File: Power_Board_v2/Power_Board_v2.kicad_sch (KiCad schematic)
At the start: 33 parts, among them J1 Conn_02x16_Odd_Even, Q1 MMBT5551L, U2 HUSB237-AA001-DN06R, U3 BQ24074RGT, U4 INA219AxDCN SOT-23

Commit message: misc.
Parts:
- C4, C8: LCSC (none) -> C19666; Supplier Part C19666 -> (none)
- C5, C6, C7: LCSC (none) -> C15849; Supplier Part C15849 -> (none)
- D1: LCSC (none) -> C2290; Supplier Part C2290 -> (none)
- D2: LCSC (none) -> C2286; Supplier Part C2286 -> (none)
- Q1: LCSC (none) -> C2145; Supplier Part C2145 -> (none)
- R10, R16: LCSC (none) -> C25804; Supplier Part C25804 -> (none)
- R11, R12, R13, R15, R18, R9: LCSC (none) -> C22843; Supplier Part C22843 -> (none)
- R14, R17: LCSC (none) -> C333100; Supplier Part C333100 -> (none)
- R2: LCSC (none) -> C23242; Supplier Part C19666 -> (none)
- R3: LCSC (none) -> C23159; Supplier Part C23159 -> (none)
- R4: LCSC (none) -> C17471
- R7: LCSC (none) -> C25804
- U2: LCSC (none) -> C22373734; SUPPLIER PART C22373734 -> (none)
- U3: LCSC (none) -> C54313; Supplier Part C54313 -> (none)
- U4: LCSC (none) -> C87469; Supplier Part C87469 -> (none)
- USBC1: LCSC (none) -> C165948; Supplier Part C165948 -> (none)
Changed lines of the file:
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@@
 			)
 		)
+		(property "LCSC" "C25804"
+			(at 195.58 60.96 0)
+			(effects
+				(font
+					(size 1.27 1.27)
+				)
+				(hide yes)
+			)
+		)
 		(pin "2"
 		)
@@
 			)
 		)
-		(property "Supplier Part" "C25804"
+		(property "LCSC" "C25804"
 			(at 71.12 40.64 0)
 			(effects
@@
 			)
 		)
-		(property "Supplier Part" "C22843"
+		(property "LCSC" "C22843"
 			(at 148.59 53.34 0)
 			(effects
@@
 			)
 		)
-		(property "Supplier Part" "C19666"
+		(property "LCSC" "C19666"
 			(at 190.5 58.42 0)
 			(effects
@@
 			)
 		)
-		(property "Supplier Part" "C165948"
+		(property "LCSC" "C165948"
 			(at 34.29 135.89 0)
 			(effects
@@
 			)
 		)
-		(property "Supplier Part" "C15849"
+		(property "LCSC" "C15849"
 			(at 148.59 27.94 0)
 			(effects
@@
 			)
 		)
-		(property "Supplier Part" "C22843"
+		(property "LCSC" "C22843"
 			(at 148.59 48.26 0)
 			(effects
@@
 			)
 		)
-		(property "Supplier Part" "C25804"
+		(property "LCSC" "C25804"
 			(at 71.12 64.77 0)
 			(effects
@@
 			)
 		)
-		(property "Supplier Part" "C87469"
+		(property "LCSC" "C87469"
 			(at 58.42 52.07 0)
 			(effects
@@
 			)
 		)
-		(property "Supplier Part" "C22843"
+		(property "LCSC" "C22843"
 			(at 157.48 88.9 0)
 			(effects
@@
 			)
 		)
-		(property "Supplier Part" "C2286"
+		(property "LCSC" "C2286"
 			(at 201.93 43.18 90)
 			(effects
@@
 			)
 		)
-		(property "Supplier Part" "C22843"
+		(property "LCSC" "C22843"
 			(at 201.93 35.56 0)
 			(effects
@@
 			)
 		)
+		(property "LCSC" "C17471"
+			(at 143.51 76.2 0)
+			(effects
+				(font
+					(size 1.27 1.27)
+				)
+				(hide yes)
+			)
+		)
 		(pin "2"
 		)
@@
 			)
 		)
-		(property "Supplier Part" " C2145"
+		(property "LCSC" " C2145"
 			(at 154.94 67.31 0)
 			(effects
@@
 			)
 		)
-		(property "SUPPLIER PART" "C22373734"
+		(property "LCSC" "C22373734"
 			(at 81.28 137.16 0)
 			(effects
@@
 			)
 		)
-		(property "Supplier Part" "C15849"
+		(property "LCSC" "C15849"
 			(at 78.74 54.61 0)
 			(effects
@@
 			)
 		)
-		(property "Supplier Part" "C23159"
+		(property "LCSC" "C23159"
 			(at 143.51 62.23 0)
 			(effects
@@
 			)
 		)
-		(property "Supplier Part" "C19666"
+		(property "LCSC" "C19666"
 			(at 218.44 39.37 0)
 			(effects
@@
 			)
 		)
-		(property "Supplier Part" "C15849"
+		(property "LCSC" "C15849"
 			(at 63.5 152.4 0)
 			(effects
@@
 			)
 		)
-		(property "Supplier Part" "C22843"
+		(property "LCSC" "C22843"
 			(at 210.82 35.56 0)
 			(effects
@@
 			)
 		)
-		(property "Supplier Part" "C22843"
+		(property "LCSC" "C22843"
 			(at 139.7 67.31 0)
 			(effects
@@
 			)
 		)
-		(property "Supplier Part" "C2290"
+		(property "LCSC" "C2290"
 			(at 210.82 43.18 90)
 			(effects
@@
 			)
 		)
-		(property "Supplier Part" "C333100"
+		(property "LCSC" "C333100"
 			(at 33.02 52.07 0)
 			(effects
@@
 			)
 		)
-		(property "Supplier Part" "C333100"
+		(property "LCSC" "C333100"
 			(at 39.37 52.07 0)
 			(effects
@@
 			)
 		)
-		(property "Supplier Part" "C19666"
+		(property "LCSC" "C23242"
 			(at 71.12 152.4 0)
 			(effects
@@
 			)
 		)
-		(property "Supplier Part" "C54313"
+		(property "LCSC" "C54313"
 			(at 173.99 40.64 90)
 			(effects

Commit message: Test
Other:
- note added: "test"
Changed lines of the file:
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@@
+		)
+	)
+	(text "test\n"
+		(exclude_from_sim no)
+		(at 267.97 260.35 0)
+		(effects
+			(font
+				(size 1.27 1.27)
+			)
 		)
 	)

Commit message: Did some PCB work
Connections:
- net BATT: now also R14.1, R17.2, TP1.1, U4.1 (IN+)
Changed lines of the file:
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@@
+		)
+	)
+	(label "BATT"
+		(at 35.56 33.02 0)
+		(effects
+			(font
+				(size 1.27 1.27)
+			)
+			(justify left bottom)
 		)
 	)

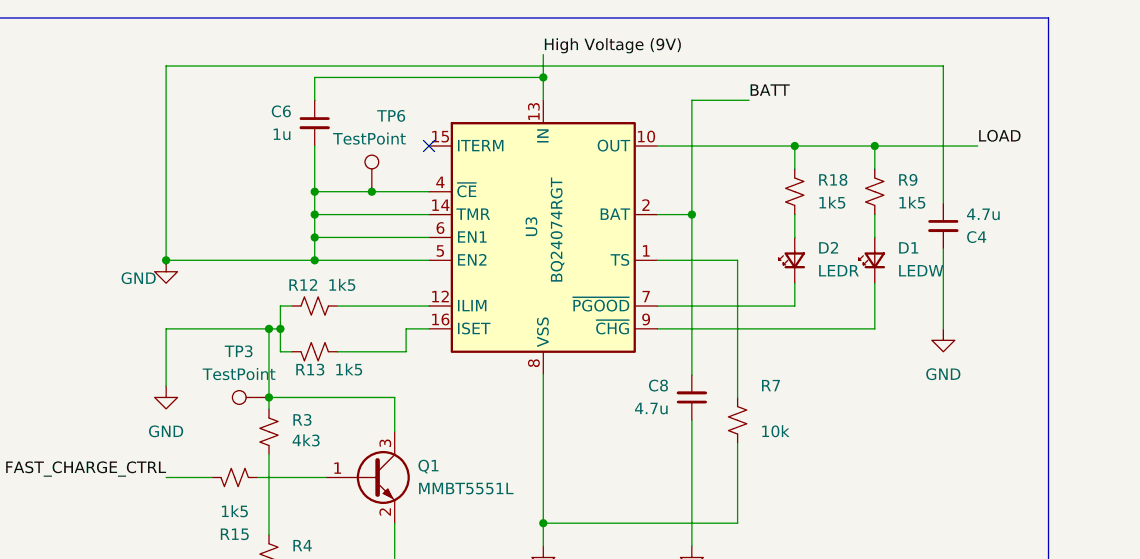
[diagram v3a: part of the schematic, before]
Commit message: Updated footprints and battery label
I HATE THE IMPERIAL SYSTEM
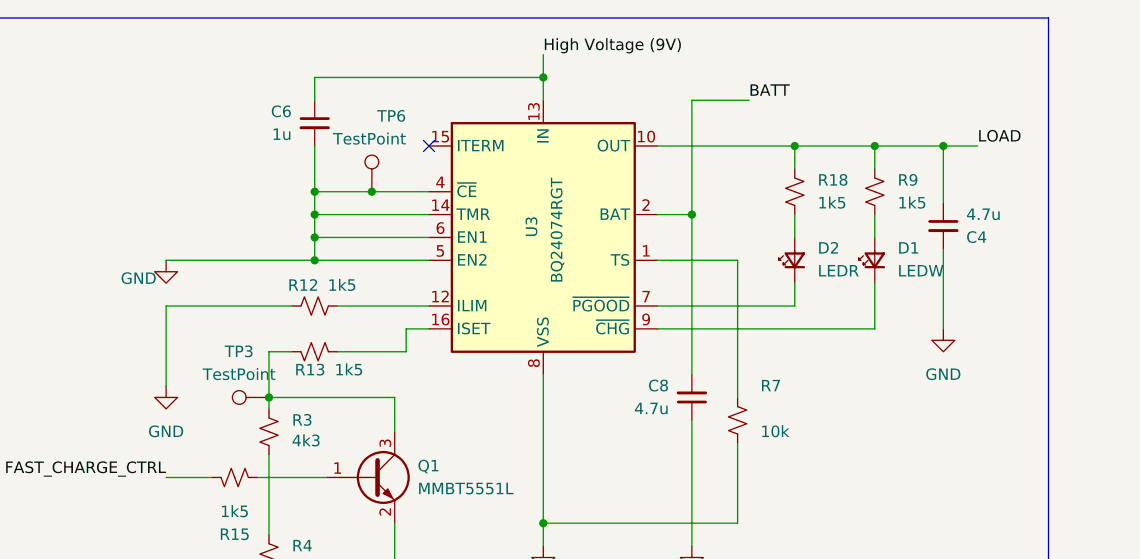
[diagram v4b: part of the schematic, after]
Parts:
- C4, C5, C6, C7, C8: footprint Capacitor_SMD:C_0201_0603Metric_Pad0.64x0.40mm_HandSolder -> Capacitor_SMD:C_0603_1608Metric_Pad1.08x0.95mm_HandSolder
- D1, D2: footprint LED_SMD:LED_0201_0603Metric_Pad0.64x0.40mm_HandSolder -> LED_SMD:LED_0603_1608Metric_Pad1.05x0.95mm_HandSolder
- R10, R11, R12, R13, R15, R16, R18, R2, R3, R7, R9: footprint Resistor_SMD:R_0201_0603Metric_Pad0.64x0.40mm_HandSolder -> Resistor_SMD:R_0603_1608Metric_Pad0.98x0.95mm_HandSolder
- R14, R17: footprint Resistor_SMD:R_0805_2012Metric_Pad1.20x1.40mm_HandSolder -> Resistor_SMD:R_1206_3216Metric_Pad1.30x1.75mm_HandSolder
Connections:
- net GND: no longer C4.1, Q1.3 (C), R13.1, R3.1, TP3.1
- net LOAD: now also C4.1
- new net: Q1.3 (C), R13.1, R3.1, TP3.1
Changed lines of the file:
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@@
 	)
 	(junction
-		(at 132.08 43.18)
-		(diameter 0)
-		(color 0 0 0 0)
-	)
-	(junction
 		(at 154.94 35.56)
 		(diameter 0)
@@
 	)
 	(junction
-		(at 143.51 50.8)
-		(diameter 0)
-		(color 0 0 0 0)
-	)
-	(junction
 		(at 36.83 163.83)
 		(diameter 0)
@@
 	)
 	(junction
-		(at 144.78 50.8)
-		(diameter 0)
-		(color 0 0 0 0)
-	)
-	(junction
 		(at 34.29 106.68)
 		(diameter 0)
@@
 	)
 	(junction
+		(at 218.44 30.48)
+		(diameter 0)
+		(color 0 0 0 0)
+	)
+	(junction
 		(at 63.5 163.83)
 		(diameter 0)
@@
 	(wire
 		(pts
-			(xy 143.51 50.8) (xy 132.08 50.8)
-		)
-		(stroke
-			(width 0)
-			(type default)
-		)
-	)
-	(wire
-		(pts
 			(xy 148.59 40.64) (xy 161.29 40.64)
 		)
@@
 	(wire
 		(pts
-			(xy 132.08 21.59) (xy 218.44 21.59)
+			(xy 190.5 74.93) (xy 190.5 60.96)
 		)
 		(stroke
@@
 	(wire
 		(pts
-			(xy 190.5 74.93) (xy 190.5 60.96)
+			(xy 190.5 25.4) (xy 190.5 38.1)
 		)
 		(stroke
@@
 	(wire
 		(pts
-			(xy 190.5 25.4) (xy 190.5 38.1)
+			(xy 218.44 30.48) (xy 218.44 36.83)
 		)
 		(stroke
@@
 	(wire
 		(pts
-			(xy 210.82 30.48) (xy 222.25 30.48)
+			(xy 143.51 53.34) (xy 146.05 53.34)
+		)
+		(stroke
+			(width 0)
+			(type default)
+		)
+	)
+	(wire
+		(pts
+			(xy 210.82 30.48) (xy 218.44 30.48)
 		)
 		(stroke
@@
 	(wire
 		(pts
-			(xy 144.78 50.8) (xy 143.51 50.8)
-		)
-		(stroke
-			(width 0)
-			(type default)
-		)
-	)
-	(wire
-		(pts
 			(xy 154.94 35.56) (xy 148.59 35.56)
 		)
@@
 	(wire
 		(pts
-			(xy 143.51 50.8) (xy 143.51 58.42)
-		)
-		(stroke
-			(width 0)
-			(type default)
-		)
-	)
-	(wire
-		(pts
 			(xy 67.31 33.02) (xy 71.12 33.02)
 		)
@@
 	(wire
 		(pts
-			(xy 146.05 48.26) (xy 144.78 48.26)
-		)
-		(stroke
-			(width 0)
-			(type default)
-		)
-	)
-	(wire
-		(pts
 			(xy 63.5 137.16) (xy 71.12 137.16)
 		)
@@
 	(wire
 		(pts
-			(xy 144.78 50.8) (xy 144.78 53.34)
+			(xy 143.51 53.34) (xy 143.51 58.42)
 		)
 		(stroke
@@
 	(wire
 		(pts
-			(xy 144.78 48.26) (xy 144.78 50.8)
+			(xy 36.83 163.83) (xy 45.72 163.83)
 		)
 		(stroke
@@
 	(wire
 		(pts
-			(xy 36.83 163.83) (xy 45.72 163.83)
+			(xy 218.44 30.48) (xy 222.25 30.48)
 		)
 		(stroke
@@
 	(wire
 		(pts
-			(xy 132.08 43.18) (xy 132.08 21.59)
-		)
-		(stroke
-			(width 0)
-			(type default)
-		)
-	)
-	(wire
-		(pts
 			(xy 22.86 125.73) (xy 50.8 125.73)
 		)
@@
 	(wire
 		(pts
+			(xy 132.08 48.26) (xy 146.05 48.26)
+		)
+		(stroke
+			(width 0)
+			(type default)
+		)
+	)
+	(wire
+		(pts
 			(xy 45.72 139.7) (xy 53.34 139.7)
 		)
@@
 	(wire
 		(pts
-			(xy 132.08 50.8) (xy 132.08 57.15)
-		)
-		(stroke
-			(width 0)
-			(type default)
-		)
-	)
-	(wire
-		(pts
 			(xy 71.12 67.31) (xy 71.12 69.85)
 		)
@@
 	(wire
 		(pts
-			(xy 218.44 21.59) (xy 218.44 36.83)
-		)
-		(stroke
-			(width 0)
-			(type default)
-		)
-	)
-	(wire
-		(pts
 			(xy 71.12 154.94) (xy 71.12 163.83)
 		)
@@
 	(wire
 		(pts
-			(xy 161.29 48.26) (xy 151.13 48.26)
+			(xy 132.08 48.26) (xy 132.08 57.15)
 		)
 		(stroke
@@
 	(wire
 		(pts
-			(xy 143.51 58.42) (xy 157.48 58.42)
+			(xy 161.29 48.26) (xy 151.13 48.26)
 		)
 		(stroke
@@
 	(wire
 		(pts
-			(xy 22.86 106.68) (xy 22.86 121.92)
+			(xy 143.51 58.42) (xy 157.48 58.42)
 		)
 		(stroke
@@
 	(wire
 		(pts
-			(xy 71.12 33.02) (xy 78.74 33.02)
+			(xy 22.86 106.68) (xy 22.86 121.92)
 		)
 		(stroke
@@
 	(wire
 		(pts
-			(xy 132.08 67.31) (xy 137.16 67.31)
+			(xy 71.12 33.02) (xy 78.74 33.02)
 		)
 		(stroke
@@
 	(wire
 		(pts
-			(xy 210.82 50.8) (xy 186.69 50.8)
+			(xy 132.08 67.31) (xy 137.16 67.31)
 		)
 		(stroke
@@
 	(wire
 		(pts
-			(xy 144.78 53.34) (xy 146.05 53.34)
+			(xy 210.82 50.8) (xy 186.69 50.8)
 		)
 		(stroke
@@
 			)
 		)
-		(property "Footprint" "Resistor_SMD:R_0201_0603Metric_Pad0.64x0.40mm_HandSolder"
+		(property "Footprint" "Resistor_SMD:R_0603_1608Metric_Pad0.98x0.95mm_HandSolder"
 			(at 195.58 60.96 0)
 			(effects
@@
 			)
 		)
-		(property "Footprint" "Resistor_SMD:R_0201_0603Metric_Pad0.64x0.40mm_HandSolder"
+		(property "Footprint" "Resistor_SMD:R_0603_1608Metric_Pad0.98x0.95mm_HandSolder"
 			(at 71.12 40.64 0)
 			(effects
@@
 			)
 		)
-		(property "Footprint" "Resistor_SMD:R_0201_0603Metric_Pad0.64x0.40mm_HandSolder"
+		(property "Footprint" "Resistor_SMD:R_0603_1608Metric_Pad0.98x0.95mm_HandSolder"
 			(at 148.59 53.34 0)
 			(effects
@@
 			)
 		)
-		(property "Footprint" "Capacitor_SMD:C_0201_0603Metric_Pad0.64x0.40mm_HandSolder"
+		(property "Footprint" "Capacitor_SMD:C_0603_1608Metric_Pad1.08x0.95mm_HandSolder"
 			(at 190.5 58.42 0)
 			(effects
@@
 			)
 		)
-		(property "Footprint" "Capacitor_SMD:C_0201_0603Metric_Pad0.64x0.40mm_HandSolder"
+		(property "Footprint" "Capacitor_SMD:C_0603_1608Metric_Pad1.08x0.95mm_HandSolder"
 			(at 148.59 27.94 0)
 			(effects
@@
 			)
 		)
-		(property "Footprint" "Resistor_SMD:R_0201_0603Metric_Pad0.64x0.40mm_HandSolder"
+		(property "Footprint" "Resistor_SMD:R_0603_1608Metric_Pad0.98x0.95mm_HandSolder"
 			(at 148.59 48.26 0)
 			(effects
@@
 			)
 		)
-		(property "Footprint" "Resistor_SMD:R_0201_0603Metric_Pad0.64x0.40mm_HandSolder"
+		(property "Footprint" "Resistor_SMD:R_0603_1608Metric_Pad0.98x0.95mm_HandSolder"
 			(at 71.12 64.77 0)
 			(effects
@@
 			)
 		)
-		(property "Footprint" "Resistor_SMD:R_0201_0603Metric_Pad0.64x0.40mm_HandSolder"
+		(property "Footprint" "Resistor_SMD:R_0603_1608Metric_Pad0.98x0.95mm_HandSolder"
 			(at 157.48 88.9 0)
 			(effects
@@
 			)
 		)
-		(property "Footprint" "LED_SMD:LED_0201_0603Metric_Pad0.64x0.40mm_HandSolder"
+		(property "Footprint" "LED_SMD:LED_0603_1608Metric_Pad1.05x0.95mm_HandSolder"
 			(at 201.93 43.18 90)
 			(effects
@@
 			)
 		)
-		(property "Footprint" "Resistor_SMD:R_0201_0603Metric_Pad0.64x0.40mm_HandSolder"
+		(property "Footprint" "Resistor_SMD:R_0603_1608Metric_Pad0.98x0.95mm_HandSolder"
 			(at 201.93 35.56 0)
 			(effects
@@
 			)
 		)
-		(property "Footprint" "Capacitor_SMD:C_0201_0603Metric_Pad0.64x0.40mm_HandSolder"
+		(property "Footprint" "Capacitor_SMD:C_0603_1608Metric_Pad1.08x0.95mm_HandSolder"
 			(at 78.74 54.61 0)
 			(effects
@@
 			)
 		)
-		(property "Footprint" "Resistor_SMD:R_0201_0603Metric_Pad0.64x0.40mm_HandSolder"
+		(property "Footprint" "Resistor_SMD:R_0603_1608Metric_Pad0.98x0.95mm_HandSolder"
 			(at 143.51 62.23 0)
 			(effects
@@
 			)
 		)
-		(property "Footprint" "Capacitor_SMD:C_0201_0603Metric_Pad0.64x0.40mm_HandSolder"
+		(property "Footprint" "Capacitor_SMD:C_0603_1608Metric_Pad1.08x0.95mm_HandSolder"
 			(at 218.44 39.37 0)
 			(effects
@@
 			)
 		)
-		(property "Footprint" "Capacitor_SMD:C_0201_0603Metric_Pad0.64x0.40mm_HandSolder"
+		(property "Footprint" "Capacitor_SMD:C_0603_1608Metric_Pad1.08x0.95mm_HandSolder"
 			(at 63.5 152.4 0)
 			(effects
@@
 			)
 		)
-		(property "Footprint" "Resistor_SMD:R_0201_0603Metric_Pad0.64x0.40mm_HandSolder"
+		(property "Footprint" "Resistor_SMD:R_0603_1608Metric_Pad0.98x0.95mm_HandSolder"
 			(at 210.82 35.56 0)
 			(effects
@@
 			)
 		)
-		(property "Footprint" "Resistor_SMD:R_0201_0603Metric_Pad0.64x0.40mm_HandSolder"
+		(property "Footprint" "Resistor_SMD:R_0603_1608Metric_Pad0.98x0.95mm_HandSolder"
 			(at 139.7 67.31 0)
 			(effects
@@
 			)
 		)
-		(property "Footprint" "LED_SMD:LED_0201_0603Metric_Pad0.64x0.40mm_HandSolder"
+		(property "Footprint" "LED_SMD:LED_0603_1608Metric_Pad1.05x0.95mm_HandSolder"
 			(at 210.82 43.18 90)
 			(effects
@@
 			)
 		)
-		(property "Footprint" "Resistor_SMD:R_0805_2012Metric_Pad1.20x1.40mm_HandSolder"
+		(property "Footprint" "Resistor_SMD:R_1206_3216Metric_Pad1.30x1.75mm_HandSolder"
 			(at 33.02 52.07 0)
 			(effects
@@
 			)
 		)
-		(property "Footprint" "Resistor_SMD:R_0805_2012Metric_Pad1.20x1.40mm_HandSolder"
+		(property "Footprint" "Resistor_SMD:R_1206_3216Metric_Pad1.30x1.75mm_HandSolder"
 			(at 39.37 52.07 0)
 			(effects
@@
 			)
 		)
-		(property "Footprint" "Resistor_SMD:R_0201_0603Metric_Pad0.64x0.40mm_HandSolder"
+		(property "Footprint" "Resistor_SMD:R_0603_1608Metric_Pad0.98x0.95mm_HandSolder"
 			(at 71.12 152.4 0)
 			(effects

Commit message: Updated parts' details to get correct BOM
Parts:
- U4: value INA219AxDCN SOT-23 -> INA219AIDCNR
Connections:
- net BATT renamed Battery

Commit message: Same as previous
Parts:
- J1: value Conn_02x16_Odd_Even -> PH2.54-01-16PZS; LCSC (none) -> C7501602
- USBC1: value ~ -> TYPE-C-31-M-12
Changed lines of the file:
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@@
 			)
 		)
-		(property "Value" "~"
+		(property "Value" "TYPE-C-31-M-12"
 			(at 38.6781 118.11 0)
 			(effects
@@
 			)
 		)
-		(property "Value" "Conn_02x16_Odd_Even"
+		(property "Value" "PH2.54-01-16PZS"
 			(at 369.57 22.86 0)
 			(effects
@@
 			)
 		)
-		(property "Supplier Part" ""
+		(property "LCSC" "C7501602"
 			(at 368.3 44.45 0)
 			(effects

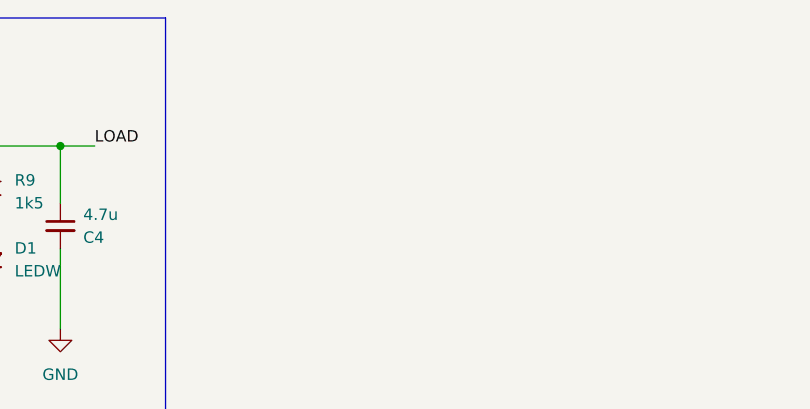
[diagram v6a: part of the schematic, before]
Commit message: Updated some stuffs
Tried to add the battery connector, but it wouldn't work
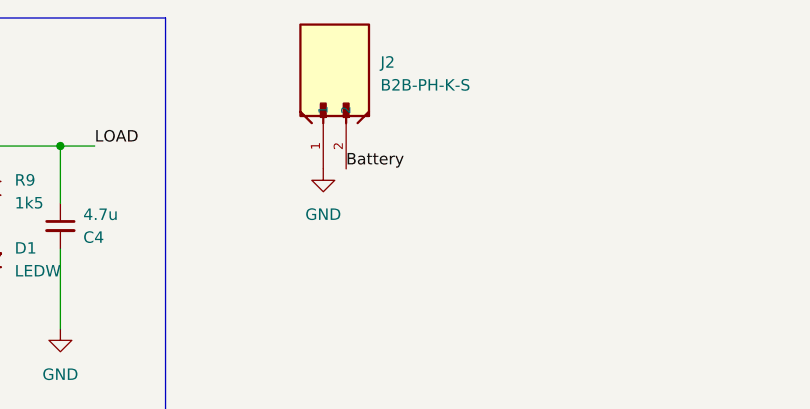
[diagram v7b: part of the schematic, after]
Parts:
- added J2: B2B-PH-K-S, B2B-PH-K-S:JST_B2B-PH-K-S, symbol B2B-PH-K-S:B2B-PH-K-S
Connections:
- net Battery: now also J2.2
- net GND: now also J2.1
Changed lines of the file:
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@@
 		)
 	)
+	(label "Battery"
+		(at 250.19 33.02 0)
+		(effects
+			(font
+				(size 1.27 1.27)
+			)
+			(justify left bottom)
+		)
+	)
 	(label "I2C1_SCL"
 		(at 375.92 44.45 0)
@@
 	)
 	(symbol
+		(lib_id "power:GND")
+		(at 247.65 33.02 0)
+		(unit 1)
+		(exclude_from_sim no)
+		(in_bom yes)
+		(on_board yes)
+		(dnp no)
+		(fields_autoplaced yes)
+		(property "Reference" "#PWR01"
+			(at 247.65 39.37 0)
+			(effects
+				(font
+					(size 1.27 1.27)
+				)
+				(hide yes)
+			)
+		)
+		(property "Value" "GND"
+			(at 247.65 38.1 0)
+			(effects
+				(font
+					(size 1.27 1.27)
+				)
+			)
+		)
+		(property "Footprint" ""
+			(at 247.65 33.02 0)
+			(effects
+				(font
+					(size 1.27 1.27)
+				)
+				(hide yes)
+			)
+		)
+		(property "Datasheet" ""
+			(at 247.65 33.02 0)
+			(effects
+				(font
+					(size 1.27 1.27)
+				)
+				(hide yes)
+			)
+		)
+		(property "Description" "Power symbol creates a global label with name \"GND\" , ground"
+			(at 247.65 33.02 0)
+			(effects
+				(font
+					(size 1.27 1.27)
+				)
+				(hide yes)
+			)
+		)
+		(pin "1"
+		)
+		(instances
+			(project ""
+				(path "/8b599c6b-a1a2-404a-83f5-7d296d952c7d"
+					(reference "#PWR01")
+					(unit 1)
+				)
+			)
+		)
+	)
+	(symbol
 		(lib_id "Device:R_Small_US")
 		(at 157.48 88.9 0)
@@
 					(unit 1)
 				)
+			)
+		)
+	)
+	(symbol
+		(lib_id "B2B-PH-K-S:B2B-PH-K-S")
+		(at 250.19 22.86 90)
+		(unit 1)
+		(exclude_from_sim no)
+		(in_bom yes)
+		(on_board yes)
+		(dnp no)
+		(property "Reference" "J2"
+			(at 254 21.193 90)
+			(effects
+				(font
+					(size 1.27 1.27)
+				)
+				(justify right)
+			)
+		)
+		(property "Value" "B2B-PH-K-S"
+			(at 254 23.733 90)
+			(effects
+				(font
+					(size 1.27 1.27)
+				)
+				(justify right)
+			)
+		)
+		(property "Footprint" "B2B-PH-K-S:JST_B2B-PH-K-S"
+			(at 250.19 22.86 0)
+			(effects
+				(font
+					(size 1.27 1.27)
+				)
+				(justify bottom)
+				(hide yes)
+			)
+		)
+		(property "Datasheet" ""
+			(at 250.19 22.86 0)
+			(effects
+				(font
+					(size 1.27 1.27)
+				)
+				(hide yes)
+			)
+		)
+		(property "Description" ""
+			(at 250.19 22.86 0)
+			(effects
+				(font
+					(size 1.27 1.27)
+				)
+				(hide yes)
+			)
+		)
+		(property "MF" "JST Sales"
+			(at 250.19 22.86 0)
+			(effects
+				(font
+					(size 1.27 1.27)
+				)
+				(justify bottom)
+				(hide yes)
+			)
+		)
+		(property "Description_1" "Connector Header Through Hole 2 position 0.079 (2.00mm)"
+			(at 250.19 22.86 0)
+			(effects
+				(font
+					(size 1.27 1.27)
+				)
+				(justify bottom)
+				(hide yes)
+			)
+		)
+		(property "Package" "None"
+			(at 250.19 22.86 0)
+			(effects
+				(font
+					(size 1.27 1.27)
+				)
+				(justify bottom)
+				(hide yes)
+			)
+		)
+		(property "Price" "None"
+			(at 250.19 22.86 0)
+			(effects
+				(font
+					(size 1.27 1.27)
+				)
+				(justify bottom)
+				(hide yes)
+			)
+		)
+		(property "Check_prices" "https://www.snapeda.com/parts/B2B-PH-K-S/JST/view-part/?ref=eda"
+			(at 250.19 22.86 0)
+			(effects
+				(font
+					(size 1.27 1.27)
+				)
+				(justify bottom)
+				(hide yes)
+			)
+		)
+		(property "SnapEDA_Link" "https://www.snapeda.com/parts/B2B-PH-K-S/JST/view-part/?ref=snap"
+			(at 250.19 22.86 0)
+			(effects
+				(font
+					(size 1.27 1.27)
+				)
+				(justify bottom)
+				(hide yes)
+			)
+		)
+		(property "MP" "B2B-PH-K-S"
+			(at 250.19 22.86 0)
+			(effects
+				(font
+					(size 1.27 1.27)
+				)
+				(justify bottom)
+				(hide yes)
+			)
+		)
+		(property "Availability" "In Stock"
+			(at 250.19 22.86 0)
+			(effects
+				(font
+					(size 1.27 1.27)
+				)
+				(justify bottom)
+				(hide yes)
+			)
+		)
+		(property "MANUFACTURER" "JST"
+			(at 250.19 22.86 0)
+			(effects
+				(font
+					(size 1.27 1.27)
+				)
+				(justify bottom)
+				(hide yes)
+			)
+		)
+		(pin "1"
+		)
+		(pin "2"
+		)
+		(instances
+			(project ""
+				(path "/8b599c6b-a1a2-404a-83f5-7d296d952c7d"
+					(reference "J2")
+					(unit 1)
+				)

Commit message: Minor tweaks
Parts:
- removed J2: B2B-PH-K-S, B2B-PH-K-S:JST_B2B-PH-K-S, symbol B2B-PH-K-S:B2B-PH-K-S
- added J2: Conn_01x02, Connector_JST:JST_PH_S2B-PH-K_1x02_P2.00mm_Horizontal, symbol Connector_Generic:Conn_01x02
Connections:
- net Battery: now also J2.1 (Pin_1)
- net GND: now also J2.2 (Pin_2); no longer C6.2, TP6.1, U3.14 (TMR), U3.4 (~{CE}), U3.5 (EN2), U3.6 (EN1)
- net LOAD: now also U3.5 (EN2)
- new net: C6.2, TP6.1, U3.14 (TMR), U3.4 (~{CE}), U3.6 (EN1)
